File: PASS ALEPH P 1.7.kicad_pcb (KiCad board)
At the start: 6 copper layers, 200 x 100 mm, 80 parts, among them Q11 BCP56-16,115, Q12 BCP56-16,115, Q2 BCX53-16,115, Q3 IRF610PBF, Q4 IRF610PBF, Q5 IRF9610PBF, Q6 IRF9610PBF, Q7 IRF610PBF, Q8 IRF610PBF, Q9 BCX53-16,115

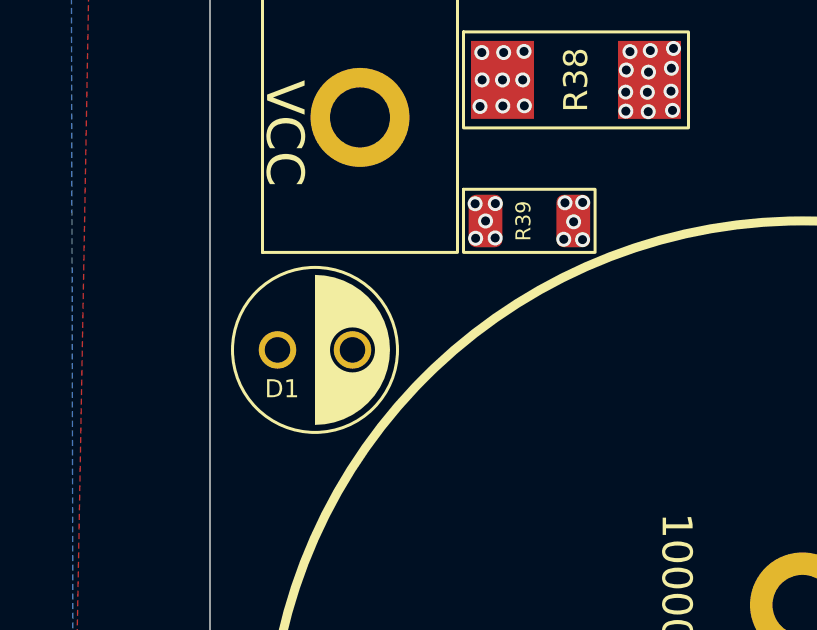
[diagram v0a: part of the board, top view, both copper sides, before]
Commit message: use smd led
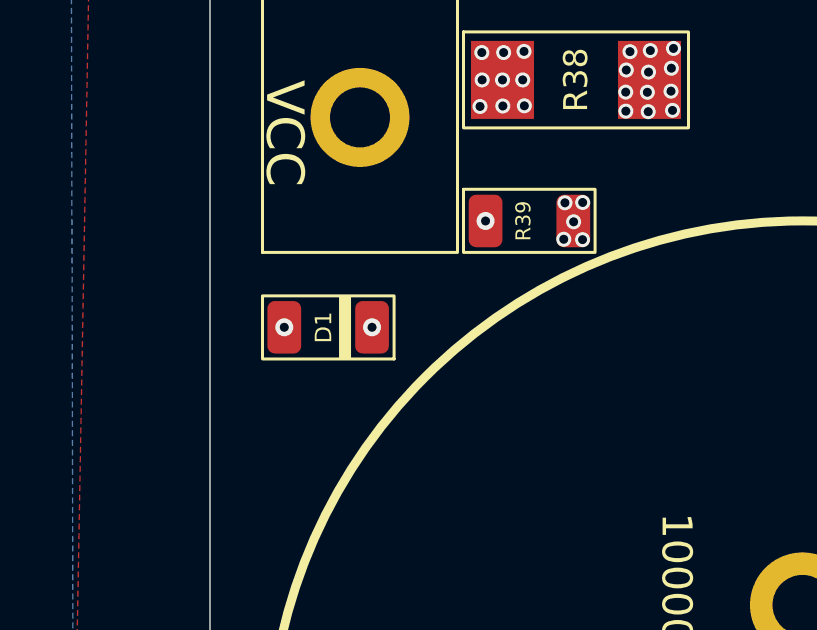
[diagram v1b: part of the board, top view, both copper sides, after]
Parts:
- D1: value NCD0603G1 -> LED; footprint generic package:LED -> generic package:LED_1206
- moved D1 3.24 mm to (25.2, 102.2), turned to 180 degrees
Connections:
- D1 pad 1: /VCC -> Net-(D1-K)
- D1 pad 2: Net-(D1-K) -> /VCC
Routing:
- net Net-(D1-K): track 6.36 -> 5.23 mm, vias 5 -> 2
- net /VCC: track 16.6 -> 15.8 mm, vias 9 -> 10
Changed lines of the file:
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@@
 		)
 	)
-	(footprint "generic package:LED"
+	(footprint "generic package:LED_1206"
 		(layer "F.Cu")
-		(at 22 103)
-		(descr "5MM LED BLUE 20MA 3V")
+		(at 25.151205 102.245694 180)
+		(descr "LED_1206")
+		(tags "LED handsolder")
 		(property "Reference" "D1"
-			(at 0.15 1.3 0)
-			(unlocked yes)
+			(at 1.614786 -0.006486 270)
 			(layer "F.SilkS")
 			(effects
 				(font
 					(face "终端更纱黑体-简 Nerd Semibold")
-					(size 0.6 0.6)
-					(thickness 0.1)
+					(size 0.55 0.55)
+					(thickness 0.125)
 				)
 			)
-			(render_cache "D1" 0
+			(render_cache "D1" 90
 				(polygon
 					(pts
-						(xy 21.964474 103.936255) (xy 21.98915 103.942118) (xy 22.01276 103.951349) (xy 22.034715 103.963861)
-						(xy 22.054306 103.979486) (xy 22.071099 103.997939) (xy 22.084531 104.018907) (xy 22.094585 104.041826)
-						(xy 22.101311 104.066351) (xy 22.105108 104.09158) (xy 22.106366 104.11669) (xy 22.106366 104.364315)
-						(xy 22.105108 104.389457) (xy 22.101311 104.41469) (xy 22.094587 104.439189) (xy 22.084531 104.462135)
-						(xy 22.071101 104.483109) (xy 22.054306 104.501592) (xy 22.034718 104.517188) (xy 22.01276 104.529692)
-						(xy 21.989151 104.538933) (xy 21.964474 104.544823) (xy 21.914135 104.549) (xy 21.780669 104.549)
-						(xy 21.780669 104.47514) (xy 21.865445 104.47514) (xy 21.914135 104.47514) (xy 21.943481 104.472613)
-						(xy 21.957414 104.468952) (xy 21.970775 104.462977) (xy 21.983047 104.454891) (xy 21.993856 104.444915)
-						(xy 22.010232 104.420992) (xy 22.019025 104.393295) (xy 22.021553 104.364315) (xy 22.021553 104.11669)
-						(xy 22.019025 104.087747) (xy 22.010232 104.06005) (xy 21.993856 104.036126) (xy 21.983047 104.026151)
-						(xy 21.970775 104.018064) (xy 21.957411 104.01207) (xy 21.943481 104.008429) (xy 21.914135 104.005901)
-						(xy 21.865445 104.005901) (xy 21.865445 104.47514) (xy 21.780669 104.47514) (xy 21.780669 103.932042)
-						(xy 21.914135 103.932042)
+						(xy 23.618421 102.293331) (xy 23.641552 102.296811) (xy 23.664009 102.302975) (xy 23.685042 102.312193)
+						(xy 23.704269 102.324503) (xy 23.721212 102.339899) (xy 23.735508 102.357855) (xy 23.74697 102.377983)
+						(xy 23.755441 102.399625) (xy 23.76084 102.422245) (xy 23.764669 102.468389) (xy 23.764669 102.590733)
+						(xy 23.199124 102.590733) (xy 23.199124 102.468389) (xy 23.266828 102.468389) (xy 23.266828 102.513021)
+						(xy 23.696964 102.513021) (xy 23.696964 102.468389) (xy 23.694647 102.441489) (xy 23.691292 102.428717)
+						(xy 23.685815 102.416469) (xy 23.678402 102.40522) (xy 23.669258 102.395312) (xy 23.647328 102.3803)
+						(xy 23.621939 102.37224) (xy 23.595375 102.369923) (xy 23.368384 102.369923) (xy 23.341854 102.37224)
+						(xy 23.316465 102.3803) (xy 23.294535 102.395312) (xy 23.28539 102.40522) (xy 23.277978 102.416469)
+						(xy 23.272483 102.42872) (xy 23.269146 102.441489) (xy 23.266828 102.468389) (xy 23.199124 102.468389)
+						(xy 23.202986 102.422245) (xy 23.20836 102.399625) (xy 23.216823 102.377983) (xy 23.228292 102.357857)
+						(xy 23.242615 102.339899) (xy 23.25953 102.324505) (xy 23.27875 102.312193) (xy 23.29976 102.302977)
+						(xy 23.322241 102.296811) (xy 23.345367 102.29333) (xy 23.368384 102.292177) (xy 23.595375 102.292177)
 					)
 				)
 				(polygon
 					(pts
-						(xy 22.343074 104.549) (xy 22.343074 104.014291) (xy 22.239833 104.094048) (xy 22.196162 104.045359)
-						(xy 22.343074 103.932042) (xy 22.427008 103.932042) (xy 22.427008 104.549)
+						(xy 23.764669 102.075195) (xy 23.274519 102.075195) (xy 23.34763 102.169833) (xy 23.302998 102.209864)
+						(xy 23.199124 102.075195) (xy 23.199124 101.998255) (xy 23.764669 101.998255)
 					)
 				)
 			)
 		)
-		(property "Value" "NCD0603G1"
-			(at -0.5 5.5 0)
-			(unlocked yes)
+		(property "Value" "LED"
+			(at 0 1.83 180)
 			(layer "F.Fab")
 			(hide yes)
@@
 		)
 		(property "Datasheet" ""
-			(at -11.25 6.75 0)
-			(unlocked yes)
+			(at 0 0 180)
 			(layer "F.Fab")
 			(hide yes)
 			(effects
 				(font
-					(size 1 1)
+					(size 1.27 1.27)
 					(thickness 0.15)
 				)
@@
 		)
 		(property "Description" "5MM LED BLUE 20MA 3V"
-			(at -11.25 6.75 0)
-			(unlocked yes)
+			(at 0 0 180)
 			(layer "F.Fab")
 			(hide yes)
 			(effects
 				(font
-					(size 1 1)
+					(size 1.27 1.27)
 					(thickness 0.15)
 				)
@@
 		(sheetname "/")
 		(sheetfile "PASS ALEPH P 1.7.kicad_sch")
-		(attr through_hole)
-		(fp_circle
-			(center 1.25 0)
-			(end 4 0)
+		(attr smd)
+		(fp_rect
+			(start -0.735214 -1.056486)
+			(end 3.651205 1.047873)
 			(stroke
 				(width 0.1)
@@
 		(fp_poly
 			(pts
-				(arc
-					(start 2.5 -0.75)
-					(mid 1.75 0)
-					(end 2.5 0.75)
-				)
-				(xy 1.25 0.75) (xy 1.25 -0.75)
+				(xy 0.7 -1.05) (xy 1.1 -1.05) (xy 1.1 1.05) (xy 0.7 1.05)
 			)
 			(stroke
@@
 			(layer "F.SilkS")
 		)
-		(fp_poly
-			(pts
-				(arc
-					(start 1.25 -2.5)
-					(mid 3.75 0)
-					(end 1.25 2.5)
-				)
-				(xy 1.25 0.75)
-				(arc
-					(start 2.5 0.75)
-					(mid 3.25 0)
-					(end 2.5 -0.75)
-				)
-				(xy 1.25 -0.75)
-			)
-			(stroke
-				(width 0)
-				(type solid)
-			)
-			(fill yes)
-			(layer "F.SilkS")
+		(pad "1" smd roundrect
+			(at 0 0 180)
+			(size 1.125 1.75)
+			(layers "F.Cu" "F.Mask" "F.Paste")
+			(roundrect_rratio 0.222222)
+			(net 37 "Net-(D1-K)")
+			(pinfunction "K")
+			(pintype "passive")
 		)
-		(pad "1" thru_hole circle
-			(at 0 0)
-			(size 1.25 1.25)
-			(drill 0.85)
-			(layers "*.Cu" "*.Mask")
-			(remove_unused_layers no)
+		(pad "2" smd roundrect
+			(at 2.925 0 180)
+			(size 1.125 1.75)
+			(layers "F.Cu" "F.Mask" "F.Paste")
+			(roundrect_rratio 0.222222)
 			(net 4 "/VCC")
 			(pinfunction "A")
 			(pintype "passive")
-			(teardrops
-				(best_length_ratio 0.5)
-				(max_length 1)
-				(best_width_ratio 1)
-				(max_width 2)
-				(curved_edges no)
-				(filter_ratio 0.9)
-				(enabled yes)
-				(allow_two_segments yes)
-				(prefer_zone_connections yes)
-			)
-		)
-		(pad "2" thru_hole circle
-			(at 2.5 0)
-			(size 1.25 1.25)
-			(drill 0.85)
-			(layers "*.Cu" "*.Mask")
-			(remove_unused_layers no)
-			(net 37 "Net-(D1-K)")
-			(pinfunction "K")
-			(pintype "passive")
-			(teardrops
-				(best_length_ratio 0.5)
-				(max_length 1)
-				(best_width_ratio 1)
-				(max_width 2)
-				(curved_edges no)
-				(filter_ratio 0.9)
-				(enabled yes)
-				(allow_two_segments yes)
-				(prefer_zone_connections yes)
-			)
 		)
 		(embedded_fonts no)
-		(model "C:/Users/cheng/Documents/KiCad/9.0/3dmodels/5MM LED BLUE 3V 20MA.STEP"
+		(model "C:/Users/cheng/Documents/KiCad/3D Model/LED_1206.stp"
 			(offset
-				(xyz 1.2 0 0.2)
+				(xyz 1.45 0 0.2)
 			)
 			(scale
@@
 			)
 			(rotate
-				(xyz -90 -0 90)
+				(xyz -90 -0 -0)
 			)
 		)
@@
 		(net 4)
 	)
+	(via
+		(at 22.226205 102.245694)
+		(size 0.6)
+		(drill 0.3)
+		(layers "F.Cu" "B.Cu")
+		(net 4)
+	)
 	(segment
 		(start 28.810562 93.087718)
@@
 	)
 	(segment
-		(start 24.75 95.25)
-		(end 23.757359 96.242641)
-		(width 2)
+		(start 23.983565 96.016435)
+		(end 24.75 95.25)
+		(width 1)
 		(layer "In2.Cu")
 		(net 4)
 	)
 	(segment
-		(start 22 100.485281)
-		(end 22 103)
-		(width 2)
+		(start 28.750819 94.885452)
+		(end 30.249835 94.885452)
+		(width 1)
 		(layer "In2.Cu")
 		(net 4)
 	)
 	(segment
-		(start 28.750819 94.885452)
-		(end 30.249835 94.885452)
+		(start 22.226205 102.245694)
+		(end 22.226205 100.259076)
 		(width 1)
 		(layer "In2.Cu")
@@
 	)
 	(arc
-		(start 23.757359 96.242641)
-		(mid 22.456723 98.189181)
-		(end 22 100.485281)
-		(width 2)
+		(start 23.983565 96.016435)
+		(mid 22.682928 97.962975)
+		(end 22.226205 100.259076)
+		(width 1)
 		(layer "In2.Cu")
 		(net 4)
@@
 	(via
 		(at 28.935214 98.702127)
-		(size 0.5)
-		(drill 0.3)
-		(layers "F.Cu" "B.Cu")
-		(net 37)
-	)
-	(via
-		(at 28.604176 99.27931)
-		(size 0.5)
+		(size 0.6)
 		(drill 0.3)
 		(layers "F.Cu" "B.Cu")
@@
 	)
 	(via
-		(at 28.587882 98.127891)
-		(size 0.5)
+		(at 25.151205 102.245694)
+		(size 0.6)
 		(drill 0.3)
 		(layers "F.Cu" "B.Cu")
 		(net 37)
 	)
-	(via
-		(at 29.261353 98.12246)
-		(size 0.5)
-		(drill 0.3)
-		(layers "F.Cu" "B.Cu")
+	(segment
+		(start 25.151205 102.245694)
+		(end 25.18454 102.245694)
+		(width 1)
+		(layer "In2.Cu")
 		(net 37)
 	)
-	(via
-		(at 29.255922 99.268448)
-		(size 0.5)
-		(drill 0.3)
-		(layers "F.Cu" "B.Cu")
+	(segment
+		(start 25.538094 102.099247)
+		(end 28.935214 98.702127)
+		(width 1)
+		(layer "In2.Cu")
 		(net 37)
 	)
-	(segment
-		(start 24.5 103)
-		(end 29 98.5)
-		(width 2)
+	(arc
+		(start 25.538094 102.099247)
+		(mid 25.375882 102.207634)
+		(end 25.18454 102.245694)
+		(width 1)
 		(layer "In2.Cu")
 		(net 37)
@@
 			)
 		)
+	)
+	(zone
+		(net 4)
+		(net_name "/VCC")
+		(layer "In2.Cu")
+		(name "$teardrop_padvia$")
+		(hatch none 0.1)
+		(priority 30000)
+		(attr
+			(teardrop
+				(type padvia)
+			)
+		)
+		(connect_pads yes
+			(clearance 0)
+		)
+		(min_thickness 0.0254)
+		(filled_areas_thickness no)
+		(fill yes
+			(thermal_gap 0.5)
+			(thermal_bridge_width 0.5)
+			(island_removal_mode 1)
+			(island_area_min 10)
+		)
+		(polygon
+			(pts
+				(xy 22.613027 96.982773) (xy 23.465665 97.505274) (xy 24.664049 96.885884) (xy 24.750522 95.249148)
+				(xy 23.145877 95.583903)
+			)
+		)

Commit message: fix some bugs
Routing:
- net Net-(Q6-D): track 14.7 -> 0.00 mm
- net Net-(Q3-D): track 10.6 -> 0.00 mm
- net Net-(Q9-B): track 3.28 -> 0.00 mm
- net Net-(Z1-A): track 4.60 -> 5.88 mm, vias 0 -> 12
- net Net-(Z3-A): track 4.60 -> 5.86 mm, vias 0 -> 12
- removed copper zone on In2.Cu, net Net-(Q3-D)
- removed copper zone on In2.Cu, net Net-(Q6-D)

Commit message: fix some bugs
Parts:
- C1, C15, C16, C2: footprint 3rd package:MMKP681K3A1001 -> cus_capacitor:B83C681JN1B0120090050EOY
- moved C16 3.07 mm to (212.5, 120.5)
- moved C15 3.04 mm to (132.1, 126.2)
- moved C1 3.02 mm to (132.1, 49.2)
- moved C2 1.93 mm to (212.5, 59.9)
- moved R27 0.94 mm to (130.8, 130.1)
- moved R28 0.94 mm to (130.8, 133.1)
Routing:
- net Net-(Q9-C): track 18.6 -> 17.1 mm
- net Net-(Q6-S): track 39.2 -> 37.9 mm
- net Net-(Q6-G): track 30.6 -> 29.7 mm
- net Net-(Q5-S): track 39.3 -> 40.1 mm
